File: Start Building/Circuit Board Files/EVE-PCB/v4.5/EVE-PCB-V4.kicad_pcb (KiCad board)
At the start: 4 copper layers, 103.5 x 90.6 mm, 89 parts, among them J1 PJ-102AH, J2 2x20 Male Header, J3 1725669, Q1 UA7805CKCT, Q10 DMN10H220L-7, Q11 DMN10H220L-7, Q2 ULN2803ADWR, Q3 ULN2803ADWR, Q4 ULN2803ADWR, Q5 ULN2803ADWR, Q6 DMN10H220L-7, Q7 DMN10H220L-7, Q8 DMN10H220L-7, Q9 DMN10H220L-7, U1 PCA9685PW, U2 ADS1115IDGSR, U3 LM324DR, U7 MCP23017-E/SO, U8 MCP23017-E/SO

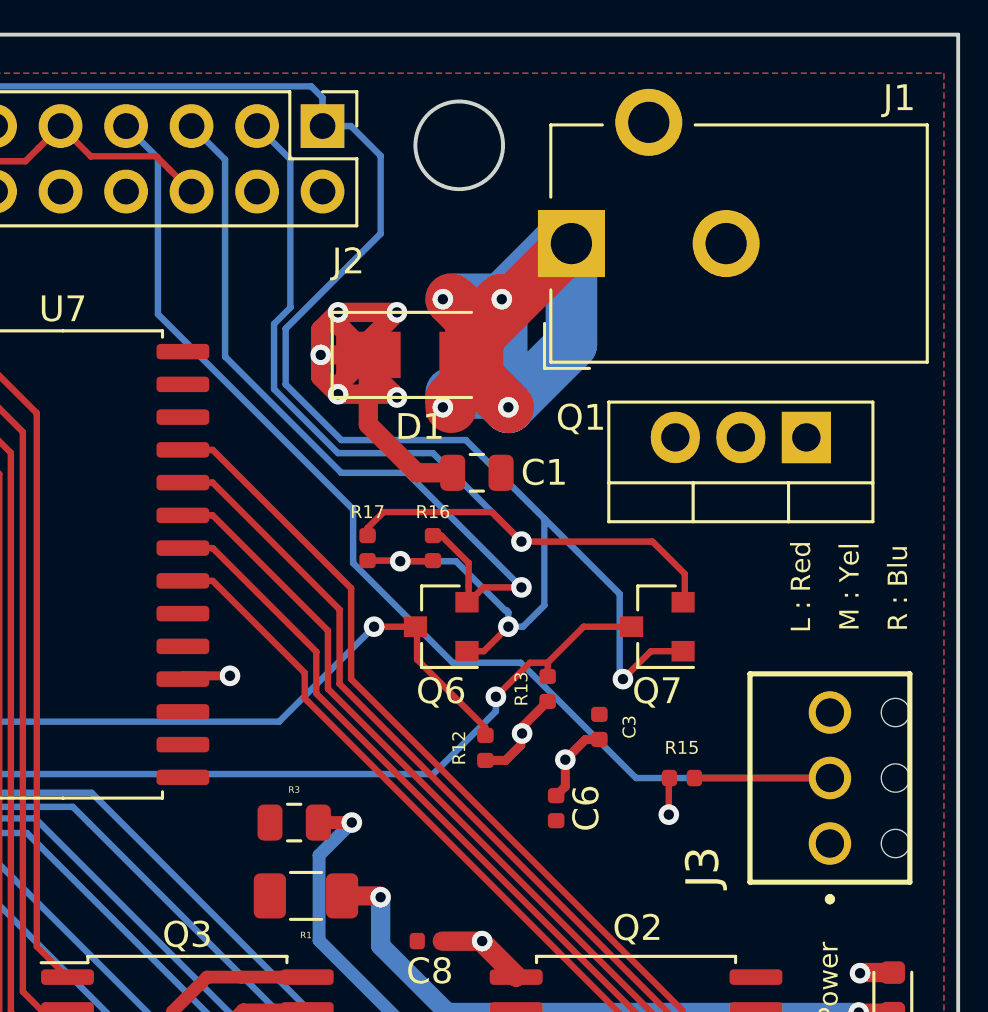
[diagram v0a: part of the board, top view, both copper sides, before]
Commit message: PCB v4.5 temp sensor PCB addition
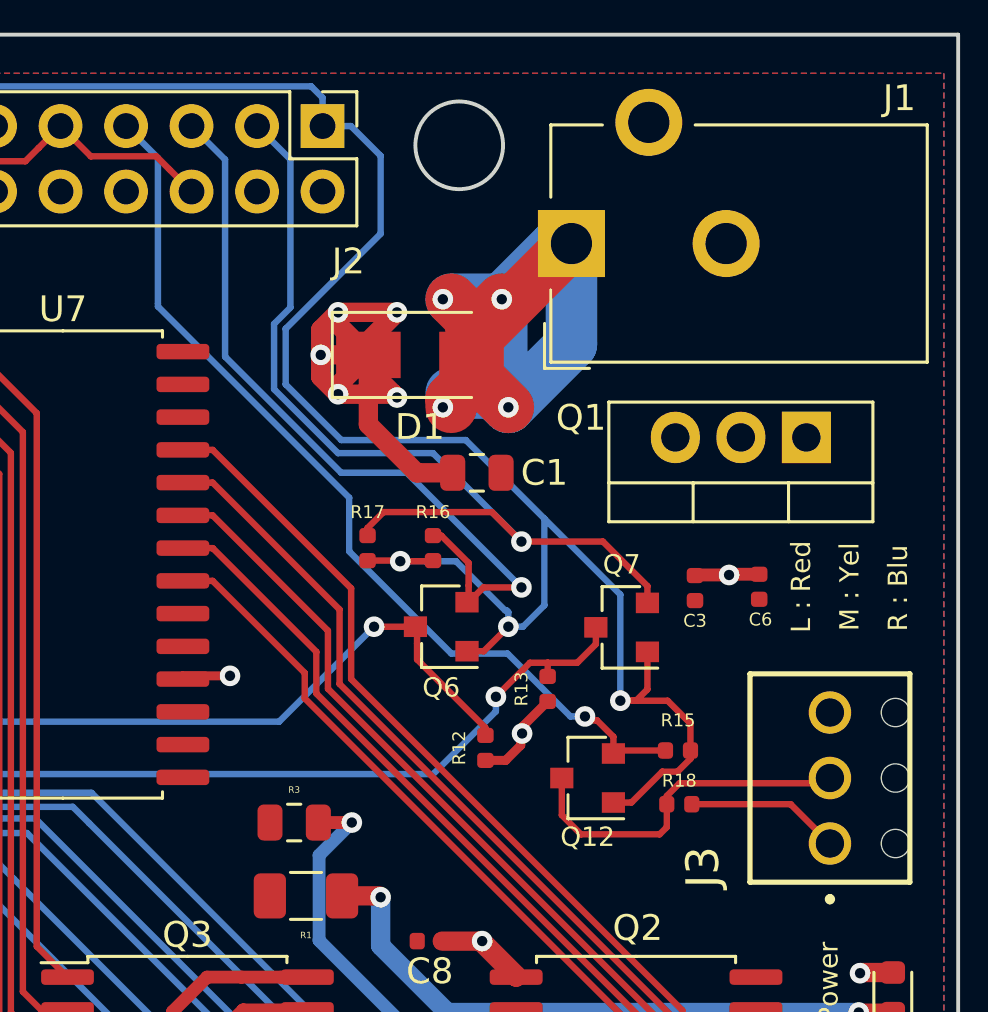
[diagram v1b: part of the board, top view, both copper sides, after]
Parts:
- added Q12: DMN10H220L-7, Package_TO_SOT_SMD:SOT-23, F.Cu at (176.7, 62.9)
- added R18: 4.7kΩ, Resistor_SMD:R_0402_1005Metric, F.Cu at (180.2, 63.9)
- moved C6 11.6 mm to (183.3, 55.5)
- moved C3 6.54 mm to (180.8, 55.5), turned to 270 degrees
- moved Q7 1.38 mm to (178.0, 57.0)
- moved R15 1.08 mm to (180.2, 61.8)
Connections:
- J2 pad 7: /TEMP_DA -> /TEMP_DA-3.3
- R15 pad 1: +5V -> /TEMP_DA-3.3
- R15 pad 2: /TEMP_DA -> +3V3
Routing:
- net /TEMP_DA-3.3: track 0.00 -> 36.0 mm, vias 0 -> 1
- net /TEMP_DA: track 47.8 -> 13.8 mm
- net +3V3: track 80.9 -> 89.7 mm
- net +5V: track 51.3 -> 55.1 mm, vias 16 -> 15
- net /SDA-3.3: track 38.0 -> 36.3 mm
- net /SDA: track 92.8 -> 91.8 mm

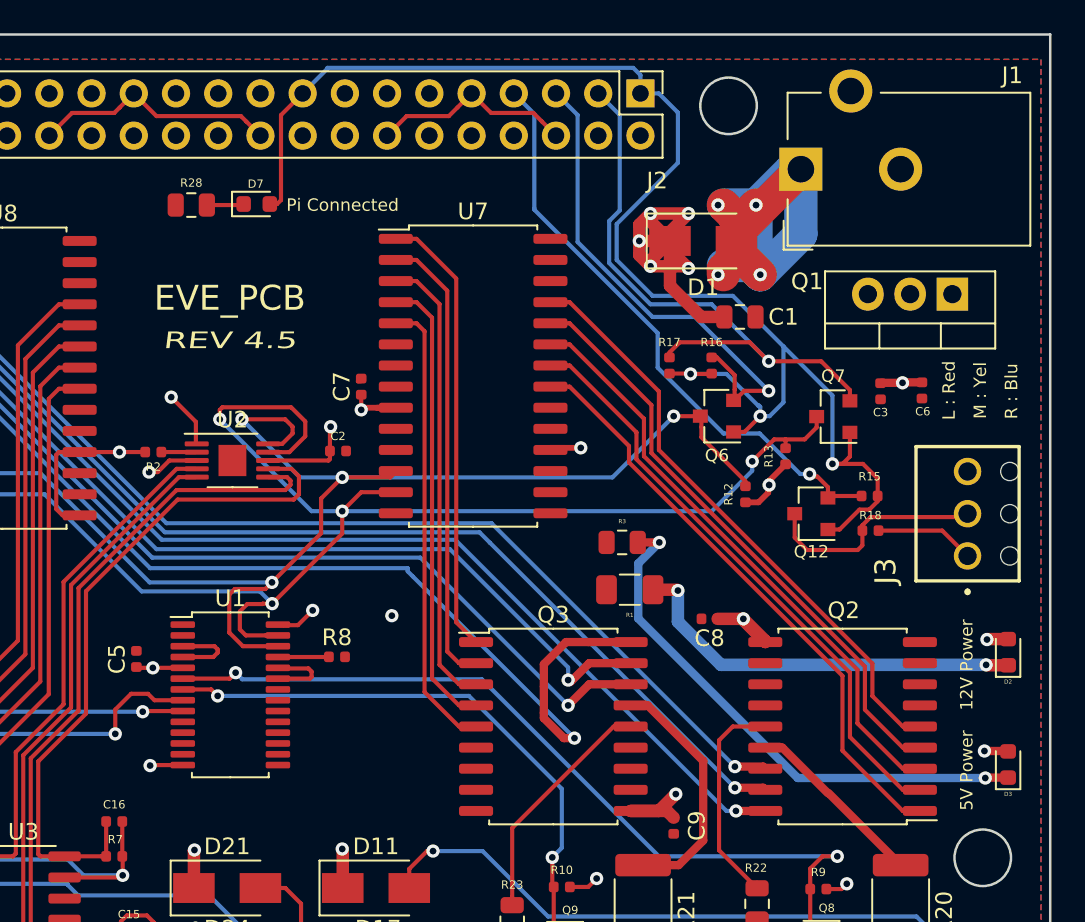
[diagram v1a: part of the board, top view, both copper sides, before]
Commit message: Updates to v4.5 and include support for ADS1115
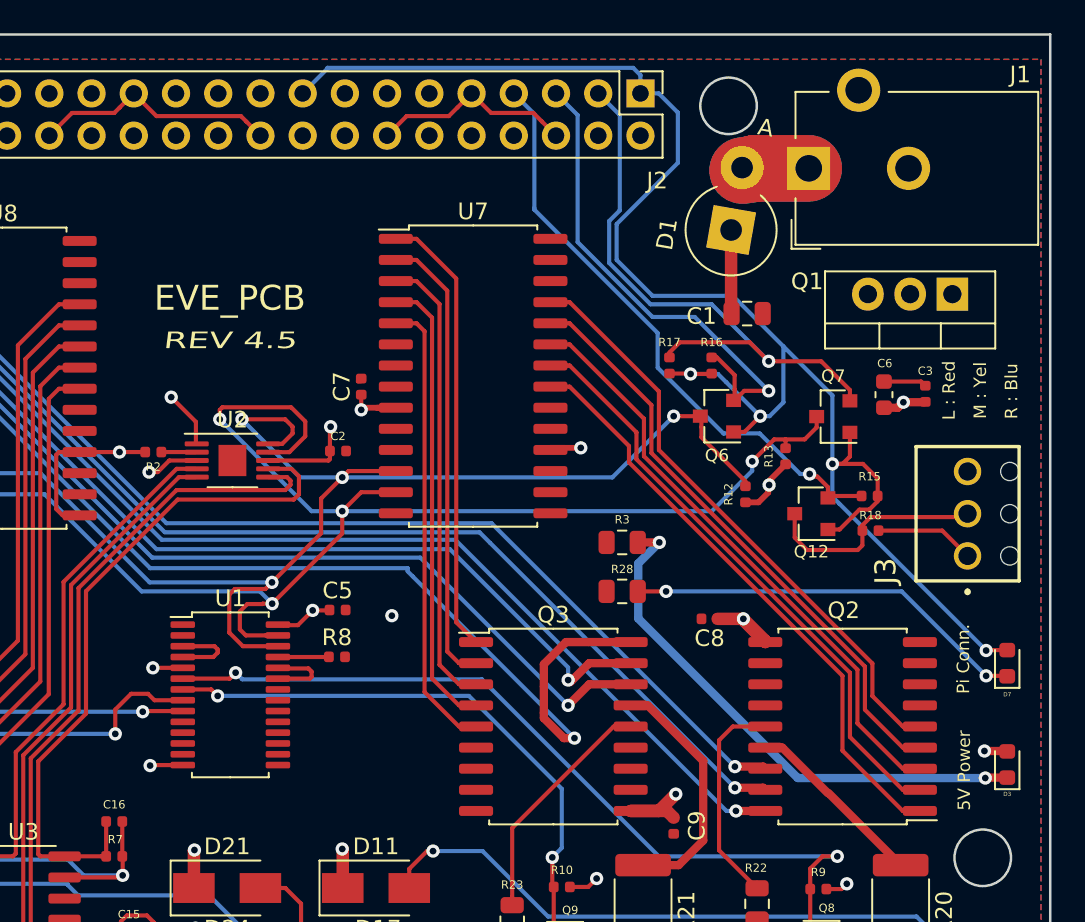
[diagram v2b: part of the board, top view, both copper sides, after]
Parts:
- removed D2: 19-217/GHC-YR1S2/3T, LED_SMD:LED_0603_1608Metric
- removed R1: 432Ω, Resistor_SMD:R_1206_3216Metric
- C6: footprint Capacitor_SMD:C_0402_1005Metric -> Capacitor_SMD:C_0603_1608Metric
- D1: value US1K-13-F -> MUR480ERLG; footprint Diode_SMD:D_SMA -> Diode_THT:D_DO-201AE_P3.81mm_Vertical_AnodeUp
- R3: value 85Ω -> 169Ω
- moved D7 52.9 mm to (188.5, 71.9), turned to 90 degrees
- moved R28 34.8 mm to (165.3, 67.6)
- moved C5 12.5 mm to (148.2, 68.7), turned to 0 degrees
- moved C3 2.70 mm to (183.5, 55.7), turned to 90 degrees
- moved C6 2.30 mm to (181.1, 55.7), turned to 90 degrees
- moved D1 1.80 mm to (171.9, 45.8), turned to 80 degrees
- moved C1 0.48 mm to (172.8, 50.9)
- moved J1 0.48 mm to (176.5, 42.1)
- moved D3 0.05 mm to (188.5, 78.0)
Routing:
- net Net-(D1-Pad2): track 48.5 -> 12.0 mm, vias 4 -> 0
- net Net-(D2-Pad1): track 24.3 -> 0.00 mm, vias 2 -> 0
- net Net-(D7-Pad1): track 2.24 -> 24.3 mm, vias 0 -> 2
- net +12V: track 87.9 -> 71.0 mm, vias 30 -> 24
- net +3V3: track 89.7 -> 98.0 mm, vias 3 -> 4
- net GND: track 54.2 -> 56.8 mm
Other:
- net class ultrabig added: clearance 0.2, trace_width 4, via_dia 0.8, via_drill 0.4
- board text added: "Pi Conn."
- board text removed: "12V Power"
- board text removed: "Pi Connected"
